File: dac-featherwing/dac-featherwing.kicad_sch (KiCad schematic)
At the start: 10 parts, among them J1 BOT, J2 TOP, J3 35RASMT4BHNTRX, U1 WM1824CGEFL

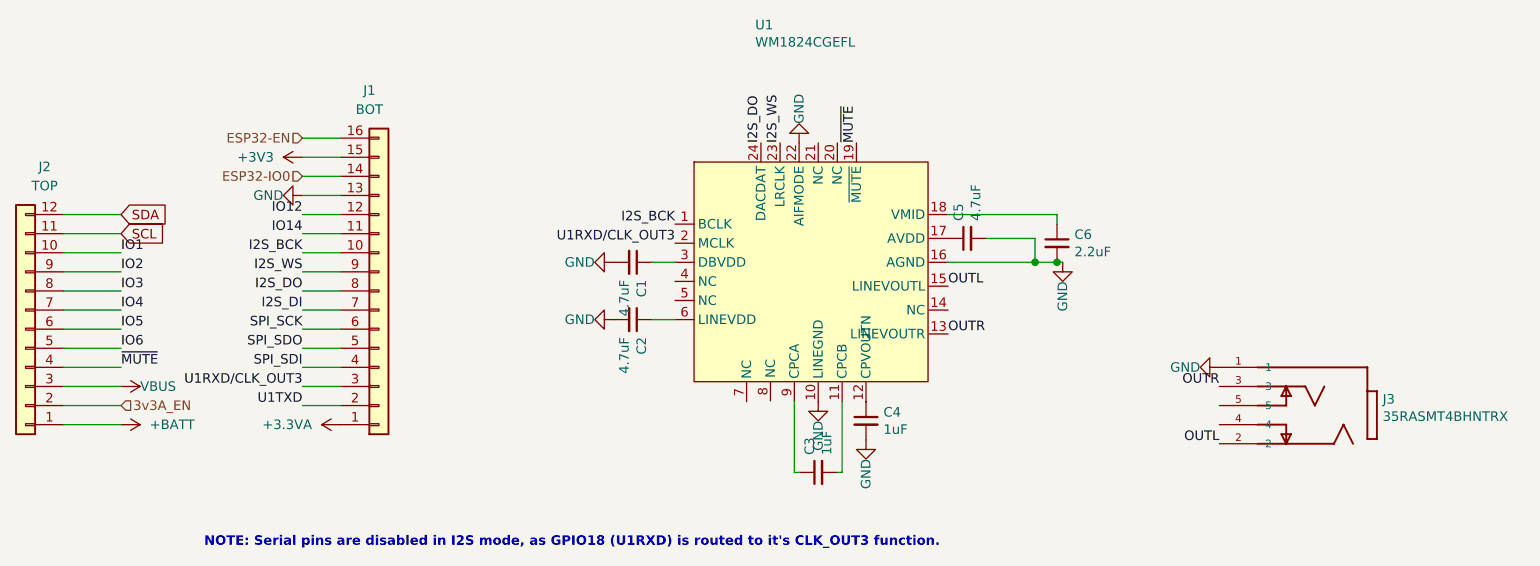
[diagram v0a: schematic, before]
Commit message: Fixed no power routed to DAC
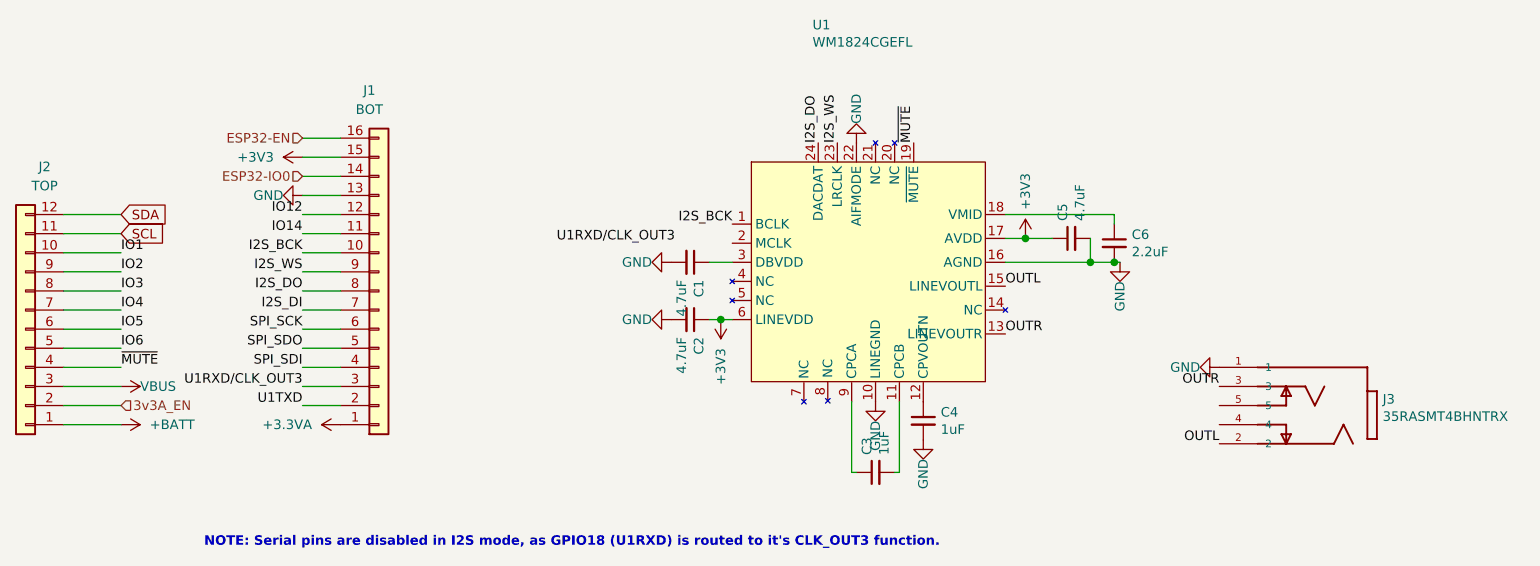
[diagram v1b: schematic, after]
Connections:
- net +3V3: now also C2.1, C5.1, U1.17 (AVDD), U1.6 (LINEVDD)
- net U1RXD/CLK_OUT3: no longer U1.2 (MCLK)
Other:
- moved on the sheet: C1, C2, C3, C4, C5, C6
